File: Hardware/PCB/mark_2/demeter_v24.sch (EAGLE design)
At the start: 65 parts, among them IC1 4050, IC2 LM1117-5.0, IC3 LM1117-3.3, IC5 MCP3424, IC6 MCP23017SO, IC8 ATMEGA32U4-AU, Q1 IRLML6402, Q2 IRLML6402, Q3 IRLML6402, Q4 IRLML6402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

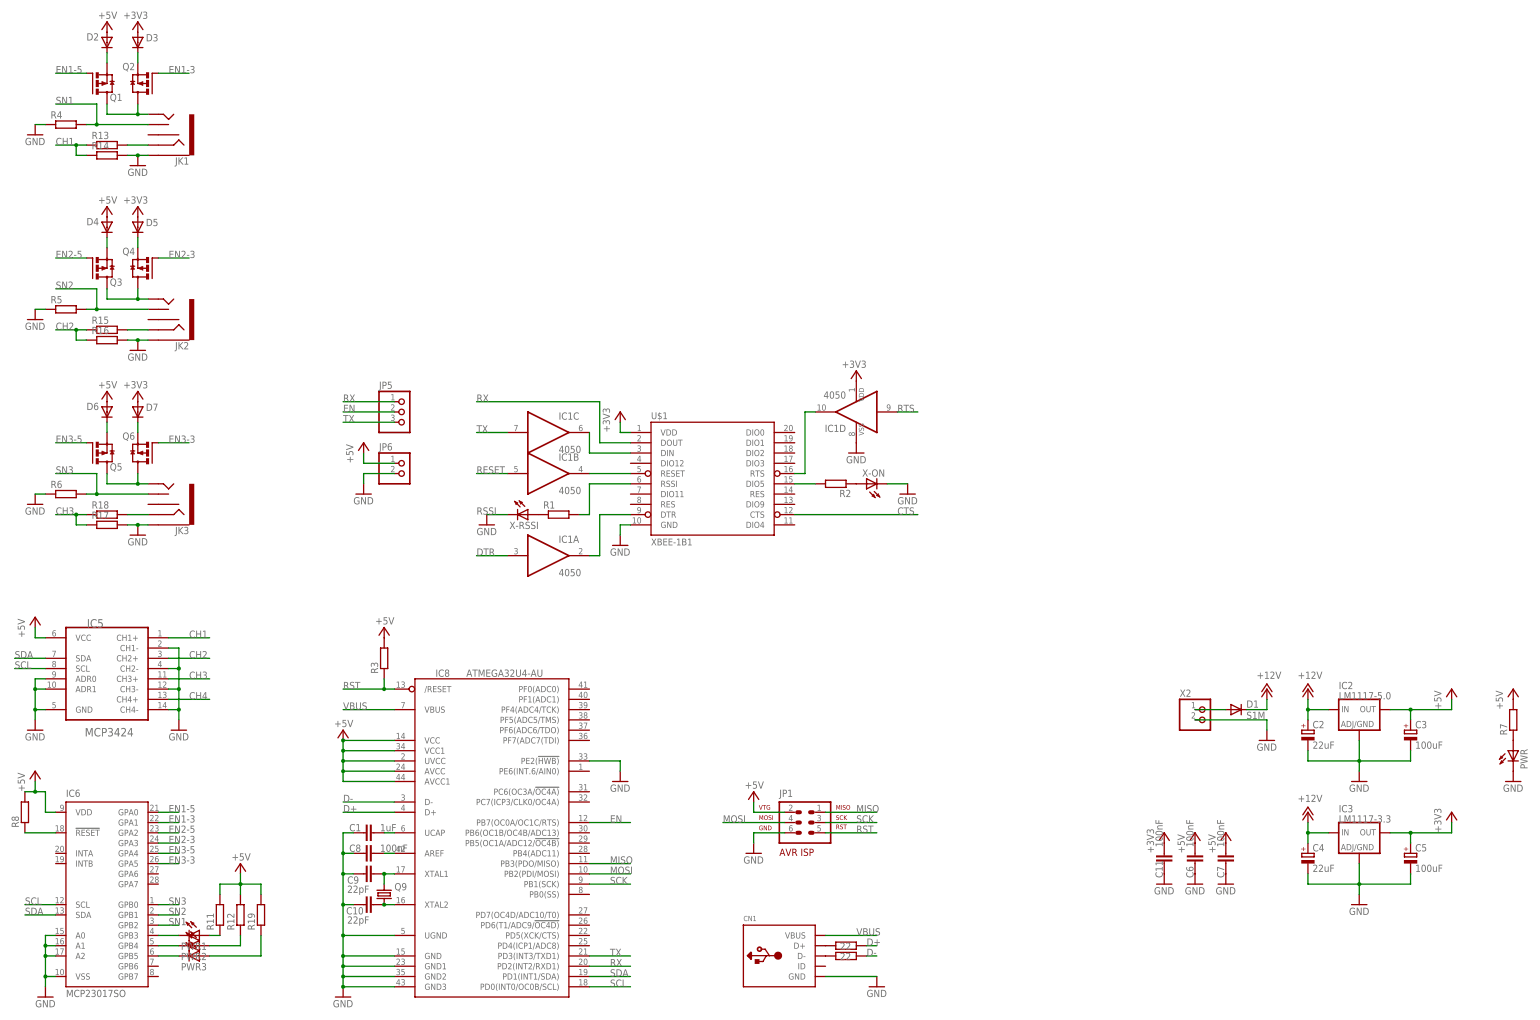
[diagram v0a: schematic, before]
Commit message: 
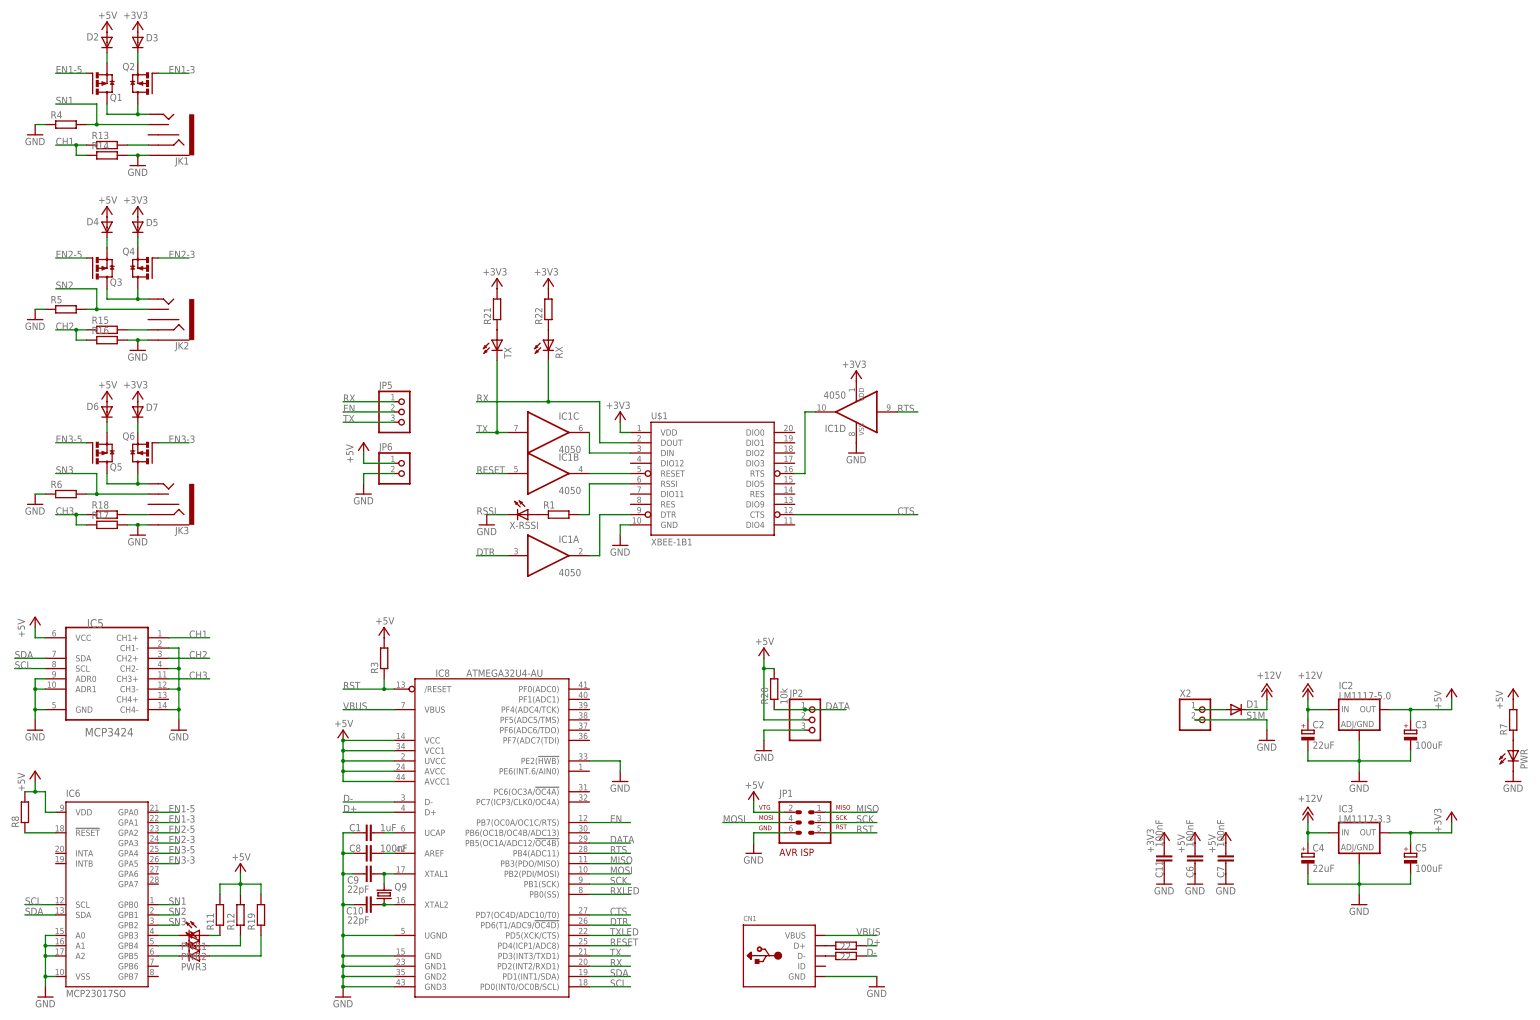
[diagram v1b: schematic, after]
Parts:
- removed R2: (no value), mark_2:R-EU_R0805
- removed X-ON: (no value), mark_2:LED0805
- added JP2: (no value), mark_2:PINHD-1X3180
- added R20: 10k, mark_2:R-EU_R0805
- added R21, R22: (no value), mark_2:R-EU_R0805
- added RX, TX: (no value), mark_2:LED0805
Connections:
- removed net CH4: IC5.CH4+
- removed net N$10: R2.2, U$1.DIO5
- removed net N$9: R2.1, X-ON.A
- new net DATA: IC8.PB5(OC1A/ADC12/!OC4B), JP2.1, R20.1
- new net N$36: R21.1, TX.A
- new net N$37: R22.1, RX.A
- new net RXLED: IC8.PB0(SS)
- new net TXLED: IC8.PD5(XCK/CTS)
- net +3V3: now also R21.2, R22.2
- net +5V: now also JP2.2, R20.2
- net CTS: now also IC8.PD7(OC4D/ADC10/T0)
- net DTR: now also IC8.PD6(T1/ADC9/!OC4D)
- net GND: now also JP2.3; no longer X-ON.C
- net RESET: now also IC8.PD4(ICP1/ADC8)
- net RTS: now also IC8.PB4(ADC11)
- net RX: now also RX.C
- net SN1: now also IC6.GPB0; no longer IC6.GPB2
- net SN3: now also IC6.GPB2; no longer IC6.GPB0
- net TX: now also TX.C
